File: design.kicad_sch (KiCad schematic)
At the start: 5 parts, among them J1 BM04B-SRSS-TB_LF__SN_, J2 BM04B-SRSS-TB_LF__SN_, SW1 SW_Push, SW2 SW_Push

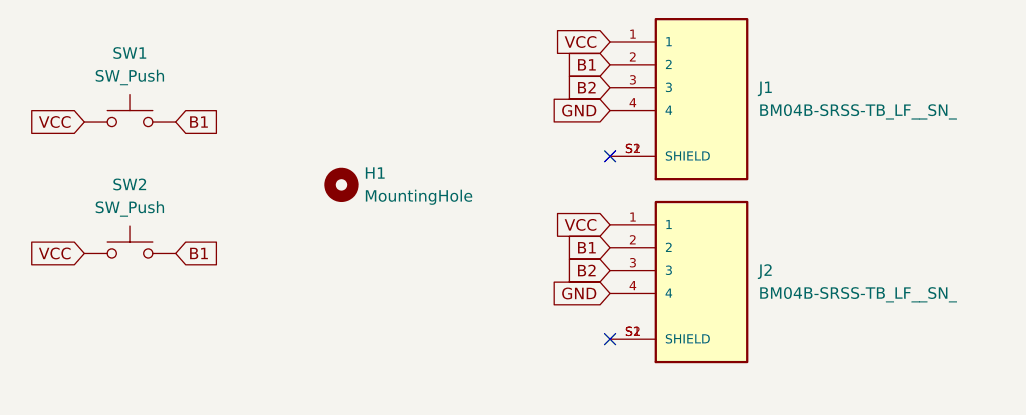
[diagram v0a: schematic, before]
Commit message: cahnge to kicad 9.x and updates
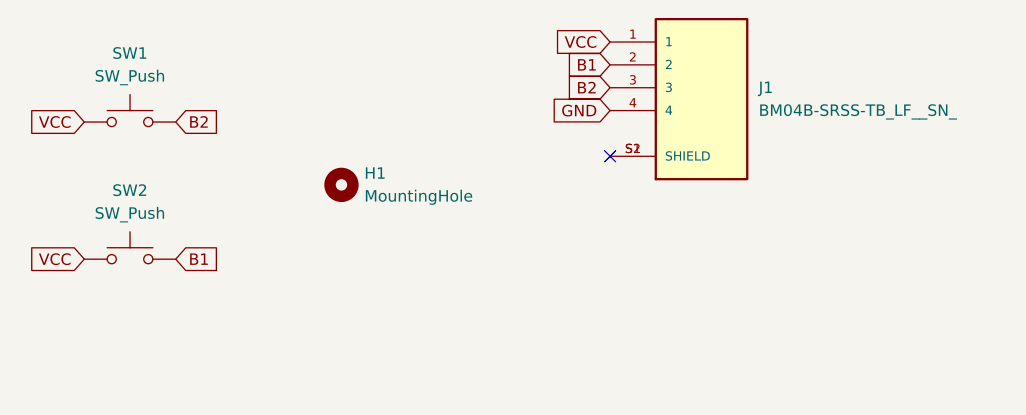
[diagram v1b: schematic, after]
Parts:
- removed J2: BM04B-SRSS-TB_LF__SN_, Snapeda:BM04B-SRSS-TB_LF__SN__JST_BM04B-SRSS-TB_LF__SN_, symbol Snapeda:BM04B-SRSS-TB_LF__SN_
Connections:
- net B1: no longer SW1.2
- net B2: now also SW1.2
- no-connect marks 2 -> 1
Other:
- moved on the sheet: SW2

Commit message: update
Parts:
- added J2: SM04B-SRSS-TB_LF__SN_, Connector_JST:JST_SH_SM04B-SRSS-TB_1x04-1MP_P1.00mm_Horizontal, symbol Snapeda:BM04B-SRSS-TB_LF__SN_
- SW1, SW2: value SW_Push -> B3F-4005
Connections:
- net B1: now also J2.2
- net B2: now also J2.3
- net GND: now also J2.4
- net VCC: now also J2.1
- new net: J2.S1 (SHIELD), J2.S2 (SHIELD)
- no-connect marks 1 -> 2
